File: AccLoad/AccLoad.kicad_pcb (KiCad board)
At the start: 2 copper layers, 59.1 x 29.1 mm, 13 parts, among them J1 to MCU

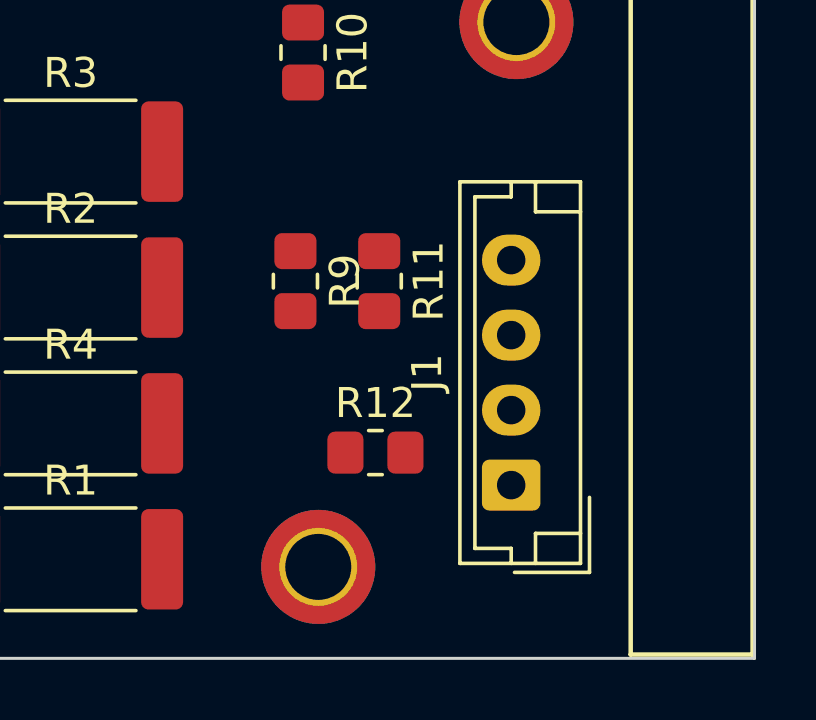
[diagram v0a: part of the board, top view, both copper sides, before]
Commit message: changed b2b
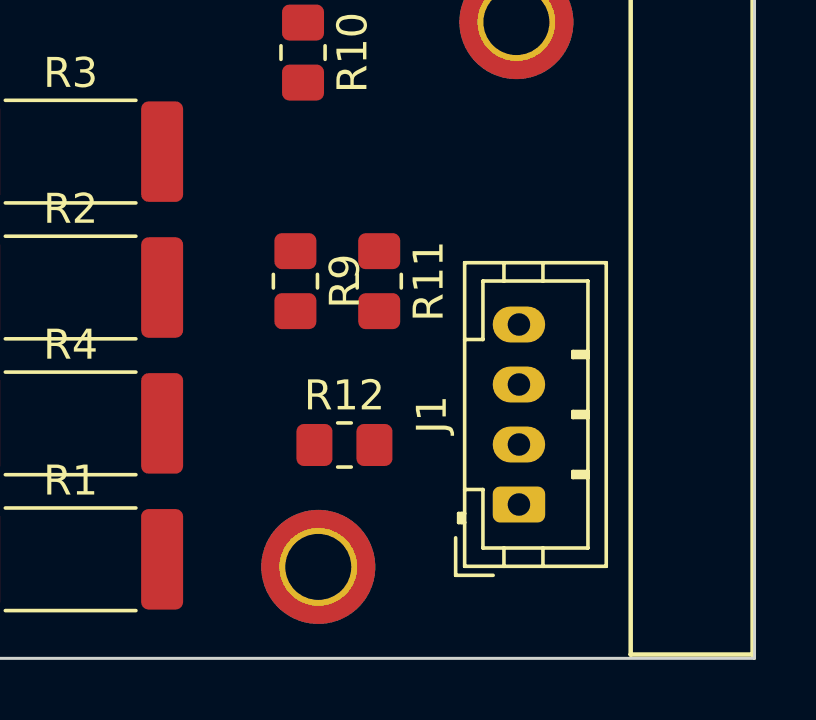
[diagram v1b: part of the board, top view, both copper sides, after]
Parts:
- J1: footprint Connector_JST:JST_EH_B4B-EH-A_1x04_P2.50mm_Vertical -> Connector_JST:JST_PH_B4B-PH-K_1x04_P2.00mm_Vertical
- moved R12 1.06 mm to (150.4, 100.3)
- moved J1 0.70 mm to (156.2, 102.3)
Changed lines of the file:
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@@
   )
   (footprint "Resistor_SMD:R_0805_2012Metric_Pad1.20x1.40mm_HandSolder" (layer "F.Cu")
-    (at 151.384 100.584)
+    (at 150.352 100.33)
     (descr "Resistor SMD 0805 (2012 Metric), square (rectangular) end terminal, IPC_7351 nominal with elongated pad for handsoldering. (Body size source: IPC-SM-782 page 72, https://www.pcb-3d.com/wordpress/wp-content/uploads/ipc-sm-782a_amendment_1_and_2.pdf), generated with kicad-footprint-generator")
     (tags "resistor handsolder")
@@
       (net 5 "Net-(H4-Pad1)") (pinfunction "1") (pintype "input"))
   )
-  (footprint "Connector_JST:JST_EH_B4B-EH-A_1x04_P2.50mm_Vertical" (layer "F.Cu")
-    (at 155.91 101.667 90)
-    (descr "JST EH series connector, B4B-EH-A (http://www.jst-mfg.com/product/pdf/eng/eEH.pdf), generated with kicad-footprint-generator")
-    (tags "connector JST EH vertical")
+  (footprint "Connector_JST:JST_PH_B4B-PH-K_1x04_P2.00mm_Vertical" (layer "F.Cu")
+    (at 156.168 102.314 90)
+    (descr "JST PH series connector, B4B-PH-K (http://www.jst-mfg.com/product/pdf/eng/ePH.pdf), generated with kicad-footprint-generator")
+    (tags "connector JST PH side entry")
     (property "Sheetfile" "AccLoad.kicad_sch")
     (property "Sheetname" "")
     (attr through_hole)
-    (fp_text reference "J1" (at 3.75 -2.8 90) (layer "F.SilkS")
-      (effects (font (size 1 1) (thickness 0.15)))
-    )
-    (fp_text value "to MCU" (at 3.75 3.4 90) (layer "F.Fab")
-      (effects (font (size 1 1) (thickness 0.15)))
-    )
-    (fp_text user "${REFERENCE}" (at 3.75 1.5 90) (layer "F.Fab")
-      (effects (font (size 1 1) (thickness 0.15)))
-    )
-    (fp_line (start -2.91 0.11) (end -2.91 2.61) (layer "F.SilkS") (width 0.12))
-    (fp_line (start 10.11 0.81) (end 9.11 0.81) (layer "F.SilkS") (width 0.12))
-    (fp_line (start -2.11 0) (end -2.11 -1.21) (layer "F.SilkS") (width 0.12))
-    (fp_line (start -2.61 0) (end -2.11 0) (layer "F.SilkS") (width 0.12))
-    (fp_line (start -2.11 -1.21) (end 9.61 -1.21) (layer "F.SilkS") (width 0.12))
-    (fp_line (start 9.61 0) (end 10.11 0) (layer "F.SilkS") (width 0.12))
-    (fp_line (start -2.61 -1.71) (end -2.61 2.31) (layer "F.SilkS") (width 0.12))
-    (fp_line (start 9.11 0.81) (end 9.11 2.31) (layer "F.SilkS") (width 0.12))
-    (fp_line (start -2.61 0.81) (end -1.61 0.81) (layer "F.SilkS") (width 0.12))
-    (fp_line (start 10.11 -1.71) (end -2.61 -1.71) (layer "F.SilkS") (width 0.12))
-    (fp_line (start -1.61 0.81) (end -1.61 2.31) (layer "F.SilkS") (width 0.12))
-    (fp_line (start -2.61 2.31) (end 10.11 2.31) (layer "F.SilkS") (width 0.12))
-    (fp_line (start 9.61 -1.21) (end 9.61 0) (layer "F.SilkS") (width 0.12))
-    (fp_line (start -2.91 2.61) (end -0.41 2.61) (layer "F.SilkS") (width 0.12))
-    (fp_line (start 10.11 2.31) (end 10.11 -1.71) (layer "F.SilkS") (width 0.12))
-    (fp_line (start -3 2.7) (end 10.5 2.7) (layer "F.CrtYd") (width 0.05))
-    (fp_line (start 10.5 -2.1) (end -3 -2.1) (layer "F.CrtYd") (width 0.05))
-    (fp_line (start -3 -2.1) (end -3 2.7) (layer "F.CrtYd") (width 0.05))
-    (fp_line (start 10.5 2.7) (end 10.5 -2.1) (layer "F.CrtYd") (width 0.05))
-    (fp_line (start 10 2.2) (end 10 -1.6) (layer "F.Fab") (width 0.1))
-    (fp_line (start -2.5 2.2) (end 10 2.2) (layer "F.Fab") (width 0.1))
-    (fp_line (start -2.91 0.11) (end -2.91 2.61) (layer "F.Fab") (width 0.1))
-    (fp_line (start -2.91 2.61) (end -0.41 2.61) (layer "F.Fab") (width 0.1))
-    (fp_line (start 10 -1.6) (end -2.5 -1.6) (layer "F.Fab") (width 0.1))
-    (fp_line (start -2.5 -1.6) (end -2.5 2.2) (layer "F.Fab") (width 0.1))
-    (pad "1" thru_hole roundrect locked (at 0 0 90) (size 1.7 1.95) (drill 0.95) (layers *.Cu *.Mask) (roundrect_rratio 0.147059)
+    (fp_text reference "J1" (at 3 -2.9 90) (layer "F.SilkS")
+      (effects (font (size 1 1) (thickness 0.15)))
+    )
+    (fp_text value "to MCU" (at 3 4 90) (layer "F.Fab")
+      (effects (font (size 1 1) (thickness 0.15)))
+    )
+    (fp_text user "${REFERENCE}" (at 3 1.5 90) (layer "F.Fab")
+      (effects (font (size 1 1) (thickness 0.15)))
+    )
+    (fp_line (start 4.9 2.3) (end 4.9 1.8) (layer "F.SilkS") (width 0.12))
+    (fp_line (start -0.3 -1.81) (end -0.3 -2.01) (layer "F.SilkS") (width 0.12))
+    (fp_line (start 8.06 2.91) (end 8.06 -1.81) (layer "F.SilkS") (width 0.12))
+    (fp_line (start 5 2.3) (end 5 1.8) (layer "F.SilkS") (width 0.12))
+    (fp_line (start -0.3 -2.01) (end -0.6 -2.01) (layer "F.SilkS") (width 0.12))
+    (fp_line (start 0.9 2.3) (end 0.9 1.8) (layer "F.SilkS") (width 0.12))
+    (fp_line (start -1.45 -1.2) (end -1.45 2.3) (layer "F.SilkS") (width 0.12))
+    (fp_line (start 1 2.3) (end 1 1.8) (layer "F.SilkS") (width 0.12))
+    (fp_line (start 1.1 1.8) (end 1.1 2.3) (layer "F.SilkS") (width 0.12))
+    (fp_line (start -2.06 -0.5) (end -1.45 -0.5) (layer "F.SilkS") (width 0.12))
+    (fp_line (start 8.06 -1.81) (end -2.06 -1.81) (layer "F.SilkS") (width 0.12))
+    (fp_line (start 7.45 -1.2) (end 5.5 -1.2) (layer "F.SilkS") (width 0.12))
+    (fp_line (start -1.11 -2.11) (end -2.36 -2.11) (layer "F.SilkS") (width 0.12))
+    (fp_line (start 5.1 1.8) (end 5.1 2.3) (layer "F.SilkS") (width 0.12))
+    (fp_line (start -2.06 2.91) (end 8.06 2.91) (layer "F.SilkS") (width 0.12))
+    (fp_line (start 8.06 -0.5) (end 7.45 -0.5) (layer "F.SilkS") (width 0.12))
+    (fp_line (start 5.5 -1.2) (end 5.5 -1.81) (layer "F.SilkS") (width 0.12))
+    (fp_line (start -2.06 0.8) (end -1.45 0.8) (layer "F.SilkS") (width 0.12))
+    (fp_line (start -1.45 2.3) (end 7.45 2.3) (layer "F.SilkS") (width 0.12))
+    (fp_line (start 3.1 1.8) (end 3.1 2.3) (layer "F.SilkS") (width 0.12))
+    (fp_line (start -2.06 -1.81) (end -2.06 2.91) (layer "F.SilkS") (width 0.12))
+    (fp_line (start 4.9 1.8) (end 5.1 1.8) (layer "F.SilkS") (width 0.12))
+    (fp_line (start 0.5 -1.81) (end 0.5 -1.2) (layer "F.SilkS") (width 0.12))
+    (fp_line (start 2.9 2.3) (end 2.9 1.8) (layer "F.SilkS") (width 0.12))
+    (fp_line (start 7.45 2.3) (end 7.45 -1.2) (layer "F.SilkS") (width 0.12))
+    (fp_line (start 3 2.3) (end 3 1.8) (layer "F.SilkS") (width 0.12))
+    (fp_line (start 8.06 0.8) (end 7.45 0.8) (layer "F.SilkS") (width 0.12))
+    (fp_line (start -0.6 -2.01) (end -0.6 -1.81) (layer "F.SilkS") (width 0.12))
+    (fp_line (start 2.9 1.8) (end 3.1 1.8) (layer "F.SilkS") (width 0.12))
+    (fp_line (start -0.3 -1.91) (end -0.6 -1.91) (layer "F.SilkS") (width 0.12))
+    (fp_line (start -2.36 -2.11) (end -2.36 -0.86) (layer "F.SilkS") (width 0.12))
+    (fp_line (start 0.5 -1.2) (end -1.45 -1.2) (layer "F.SilkS") (width 0.12))
+    (fp_line (start 0.9 1.8) (end 1.1 1.8) (layer "F.SilkS") (width 0.12))
+    (fp_line (start 8.45 3.3) (end 8.45 -2.2) (layer "F.CrtYd") (width 0.05))
+    (fp_line (start -2.45 -2.2) (end -2.45 3.3) (layer "F.CrtYd") (width 0.05))
+    (fp_line (start -2.45 3.3) (end 8.45 3.3) (layer "F.CrtYd") (width 0.05))
+    (fp_line (start 8.45 -2.2) (end -2.45 -2.2) (layer "F.CrtYd") (width 0.05))
+    (fp_line (start -2.36 -2.11) (end -2.36 -0.86) (layer "F.Fab") (width 0.1))
+    (fp_line (start -1.95 2.8) (end 7.95 2.8) (layer "F.Fab") (width 0.1))
+    (fp_line (start -1.95 -1.7) (end -1.95 2.8) (layer "F.Fab") (width 0.1))
+    (fp_line (start 7.95 2.8) (end 7.95 -1.7) (layer "F.Fab") (width 0.1))
+    (fp_line (start -1.11 -2.11) (end -2.36 -2.11) (layer "F.Fab") (width 0.1))
+    (fp_line (start 7.95 -1.7) (end -1.95 -1.7) (layer "F.Fab") (width 0.1))
+    (pad "1" thru_hole roundrect locked (at 0 0 90) (size 1.2 1.75) (drill 0.75) (layers *.Cu *.Mask) (roundrect_rratio 0.208333)
       (net 6 "unconnected-(J1-Pad1)") (pinfunction "Pin_1") (pintype "passive"))
-    (pad "2" thru_hole oval locked (at 2.5 0 90) (size 1.7 1.95) (drill 0.95) (layers *.Cu *.Mask)
+    (pad "2" thru_hole oval locked (at 2 0 90) (size 1.2 1.75) (drill 0.75) (layers *.Cu *.Mask)
       (net 4 "i1") (pinfunction "Pin_2") (pintype "passive"))
-    (pad "3" thru_hole oval locked (at 5 0 90) (size 1.7 1.95) (drill 0.95) (layers *.Cu *.Mask)
+    (pad "3" thru_hole oval locked (at 4 0 90) (size 1.2 1.75) (drill 0.75) (layers *.Cu *.Mask)
       (net 1 "bat1-") (pinfunction "Pin_3") (pintype "passive"))
-    (pad "4" thru_hole oval locked (at 7.5 0 90) (size 1.7 1.95) (drill 0.95) (layers *.Cu *.Mask)
+    (pad "4" thru_hole oval locked (at 6 0 90) (size 1.2 1.75) (drill 0.75) (layers *.Cu *.Mask)
       (net 2 "u1") (pinfunction "Pin_4") (pintype "passive"))
-    (model "${KICAD6_3DMODEL_DIR}/Connector_JST.3dshapes/JST_EH_B4B-EH-A_1x04_P2.50mm_Vertical.wrl"
-      (offset (xyz 0 0 0))
-      (scale (xyz 1 1 1))
+    (model "${KICAD6_3DMODEL_DIR}/Connector_JST.3dshapes/JST_PH_B4B-PH-K_1x04_P2.00mm_Vertical.wrl"
+      (offset (xyz 0 0 0))
+      (scale (xyz 1 1 1))

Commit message: fixed errors
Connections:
- J1 pad 1: unconnected-(J1-Pad1) -> i1
- J1 pad 2: i1 -> u1
- J1 pad 4: u1 -> unconnected-(J1-Pad4)
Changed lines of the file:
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@@
   (net 4 "i1")
   (net 5 "Net-(H4-Pad1)")
-  (net 6 "unconnected-(J1-Pad1)")
+  (net 6 "unconnected-(J1-Pad4)")
   (footprint "Resistor_SMD:R_2512_6332Metric_Pad1.40x3.35mm_HandSolder" (layer "F.Cu")
     (at 141.224 95.080666)
@@
     (fp_line (start 7.95 -1.7) (end -1.95 -1.7) (layer "F.Fab") (width 0.1))
     (pad "1" thru_hole roundrect locked (at 0 0 90) (size 1.2 1.75) (drill 0.75) (layers *.Cu *.Mask) (roundrect_rratio 0.208333)
-      (net 6 "unconnected-(J1-Pad1)") (pinfunction "Pin_1") (pintype "passive"))
+      (net 4 "i1") (pinfunction "Pin_1") (pintype "passive"))
     (pad "2" thru_hole oval locked (at 2 0 90) (size 1.2 1.75) (drill 0.75) (layers *.Cu *.Mask)
-      (net 4 "i1") (pinfunction "Pin_2") (pintype "passive"))
+      (net 2 "u1") (pinfunction "Pin_2") (pintype "passive"))
     (pad "3" thru_hole oval locked (at 4 0 90) (size 1.2 1.75) (drill 0.75) (layers *.Cu *.Mask)
       (net 1 "bat1-") (pinfunction "Pin_3") (pintype "passive"))
     (pad "4" thru_hole oval locked (at 6 0 90) (size 1.2 1.75) (drill 0.75) (layers *.Cu *.Mask)
-      (net 2 "u1") (pinfunction "Pin_4") (pintype "passive"))
+      (net 6 "unconnected-(J1-Pad4)") (pinfunction "Pin_4") (pintype "passive"))
     (model "${KICAD6_3DMODEL_DIR}/Connector_JST.3dshapes/JST_PH_B4B-PH-K_1x04_P2.00mm_Vertical.wrl"
       (offset (xyz 0 0 0))

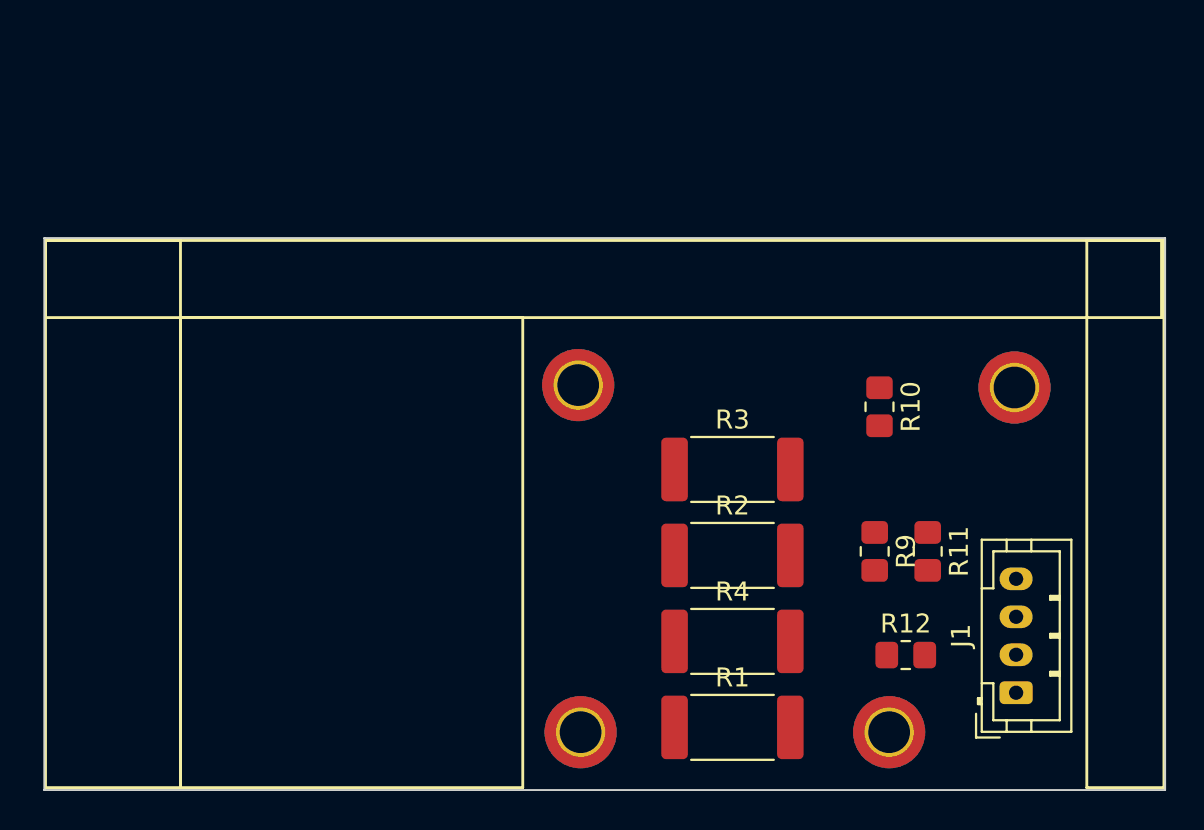
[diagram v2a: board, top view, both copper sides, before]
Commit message: PCD maked
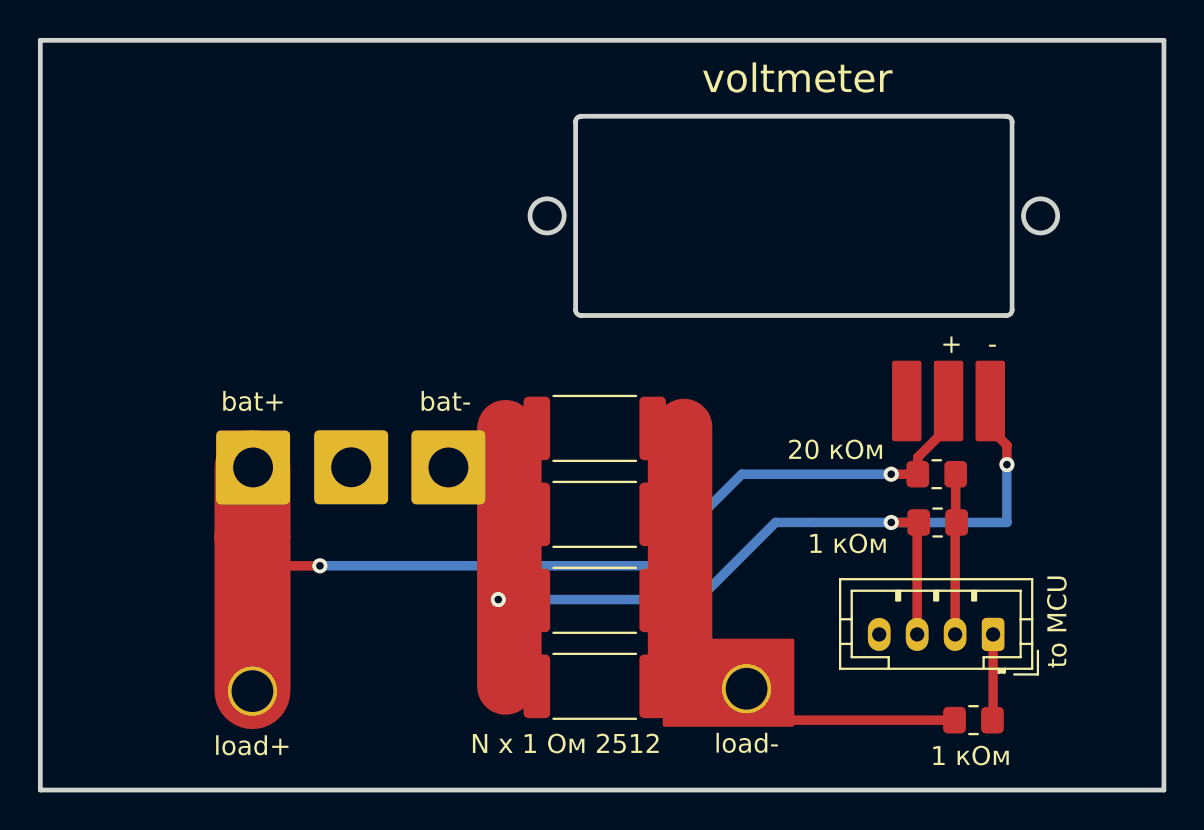
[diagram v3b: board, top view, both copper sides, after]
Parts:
- removed R9: 100 кОм*, Resistor_SMD:R_0805_2012Metric_Pad1.20x1.40mm_HandSolder
- added H2: nu, Connector_Wire:SolderWire-1.5sqmm_1x01_D1.7mm_OD3.9mm, F.Cu at (121.1, 90.4)
- H1, H2: footprint MountingHole:MountingHole_2.2mm_M2_DIN965_Pad_TopBottom -> Connector_Wire:SolderWire-1.5sqmm_1x01_D1.7mm_OD3.9mm
- R1: value 1 Ом 1 Вт -> N x 1 Ом 2512
- moved H3 43.2 mm to (115.9, 102.2)
- moved H1 17.7 mm to (116.0, 90.4)
- moved H2 15.6 mm to (126.3, 90.4)
- moved H4 7.85 mm to (142.0, 102.1)
- moved R1 7.57 mm to (134.0, 102.0)
- moved R3 7.57 mm to (134.0, 88.4)
- moved R4 7.57 mm to (134.0, 97.4)
- moved R2 7.57 mm to (134.0, 92.9)
- moved R12 4.95 mm to (153.9, 103.8)
- moved R10 4.66 mm to (152.0, 90.8), turned to 0 degrees
- moved J1 3.30 mm to (155.0, 99.2), turned to 180 degrees
- moved R11 1.61 mm to (152.0, 93.3), turned to 180 degrees
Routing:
- net bat1-: track 0.00 -> 65.3 mm, vias 0 -> 3
- net bat1+: track 0.00 -> 52.1 mm, vias 0 -> 2
- net Net-(H4-Pad1): track 0.00 -> 30.4 mm
- net u1: track 0.00 -> 8.49 mm
- net i1: track 0.00 -> 4.53 mm
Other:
- board size 59.1 x 29.1 mm -> 59.2 x 39.5 mm
- board text added: "+"
- board text added: "-"
- board text added: "voltmeter"

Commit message: fixed PCB error with voltmeter+- and border reroute
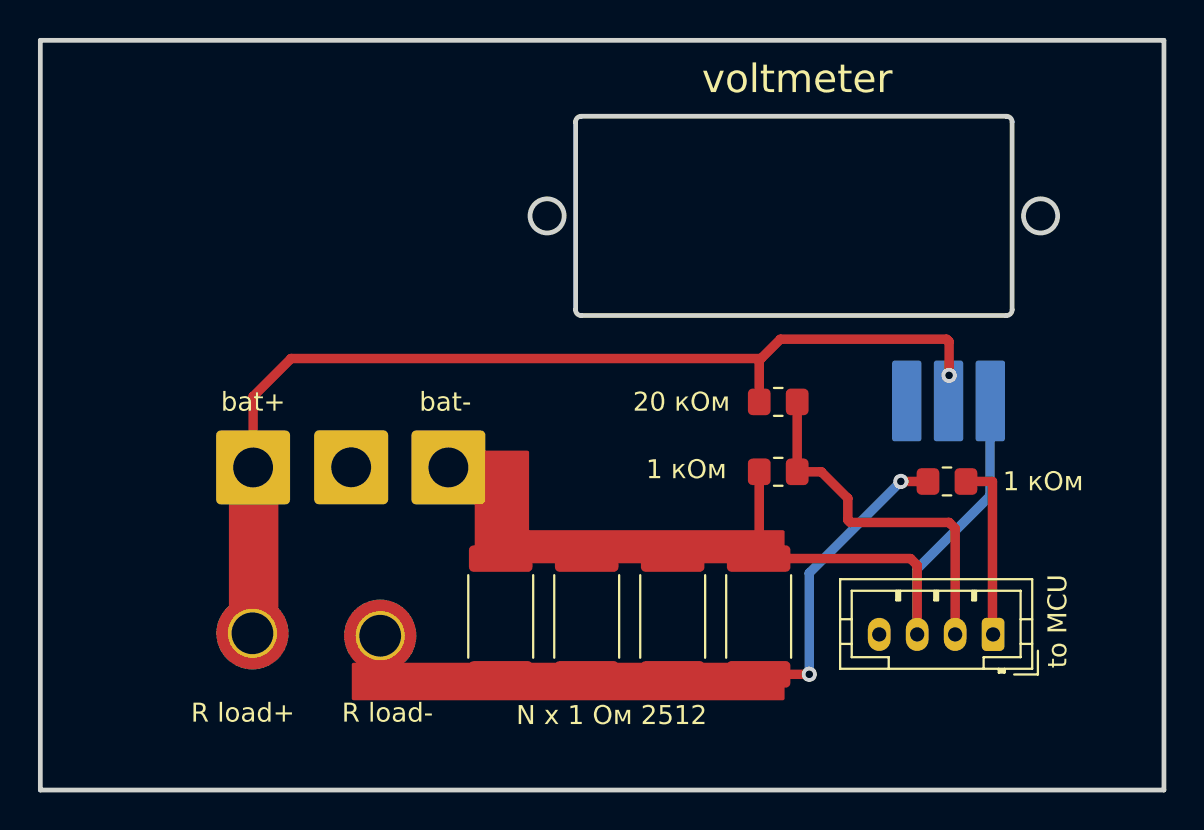
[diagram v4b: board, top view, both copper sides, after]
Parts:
- added H3: v+, Sharonov:APEX_voltmeter_pin, F.Cu at (152.6, 86.9)
- added H4: v-, Sharonov:APEX_voltmeter_pin, F.Cu at (154.8, 87.0)
- H nu: renamed from H2
- H5: renamed from H3; value load+ -> R load+
- H6: renamed from H4; value load- -> R load-
- moved H6 19.5 mm to (122.7, 99.3)
- moved R3 13.1 mm to (142.6, 98.3), turned to -90 degrees
- moved R11 12.7 mm to (152.5, 91.2)
- moved R9 9.18 mm to (143.6, 87.0)
- moved R10 8.81 mm to (143.6, 90.7)
- moved R2 6.77 mm to (138.1, 98.3), turned to -90 degrees
- moved R1 6.17 mm to (129.0, 98.3), turned to -90 degrees
- moved H5 3.05 mm to (115.9, 99.2)
- moved R4 0.95 mm to (133.5, 98.3), turned to -90 degrees
- renumbered R11 to R10, R12 to R11, R10 to R9
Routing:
- net bat1-: track 65.3 -> 50.1 mm, vias 3 -> 0
- net u1: track 8.49 -> 19.5 mm
- net Net-(H6-Pad1): track 30.4 -> 37.3 mm, vias 0 -> 2
- net i1: track 4.53 -> 9.47 mm
- net bat1+: track 52.1 -> 55.8 mm, vias 2 -> 1
